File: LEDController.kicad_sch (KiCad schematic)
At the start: 11 parts, among them J9 LED connector, Q3 2N7002K, Q4 2N7002K, Q8 2N7002K

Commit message: Schematic
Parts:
- removed R33, R47, R50: 200Ω, PCM_JLCPCB:R_0603, symbol PCM_JLCPCB-Resistors:0603,200Ω
- added Q10, Q11, Q2, Q3, Q7, Q8: MMBT2222A 1P, PCM_JLCPCB:Q_SOT-23, symbol PCM_JLCPCB-Transistors:NPN,MMBT2222A 1P
- added Q12, Q4, Q9: MMBT5401 200-300, PCM_JLCPCB:Q_SOT-23, symbol PCM_JLCPCB-Transistors:PNP,MMBT5401 200-300
- added R27, R36, R40: 1kΩ, PCM_JLCPCB:R_0402, symbol PCM_JLCPCB-Resistors:0402,1kΩ
- added R28, R32, R35: 100Ω, PCM_JLCPCB:R_0603, symbol PCM_JLCPCB-Resistors:0603,100Ω
- added R29, R37, R41: 10kΩ, PCM_JLCPCB:R_0402, symbol PCM_JLCPCB-Resistors:0402,10kΩ
- added R30, R38, R42: 330Ω, PCM_JLCPCB:R_0402, symbol PCM_JLCPCB-Resistors:0402,330Ω
- added R33, R39, R43: 47Ω, PCM_JLCPCB:R_0402, symbol PCM_JLCPCB-Resistors:0402,47Ω
- renumbered C7 to C6, J9 to J6, Q3 to Q1, Q4 to Q5, Q8 to Q6, R32 to R26, R34 to R31, R49 to R34
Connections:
- net B: now also R40.1; no longer R34.1
- net G: now also R36.1; no longer R31.1
- net GND: now also Q10.2 (E), Q12.2 (E), Q2.2 (E), Q4.2 (E), Q7.2 (E), Q9.2 (E), R29.2, R37.2, R41.2
- net R: now also R27.1; no longer R26.1
- net U_reg: now also Q11.3 (C), Q3.3 (C), Q8.3 (C), R30.1, R38.1, R42.1
- net at Q6.1 (G): now also R35.2
- net at Q5.1 (G): now also R32.2
- net at Q1.1 (G): now also R28.2
- new net: Q7.3 (C), Q8.1 (B), Q9.1 (B), R38.2
- new net: Q8.2 (E), Q9.3 (C), R39.1
- new net: Q2.3 (C), Q3.1 (B), Q4.1 (B), R30.2
- new net: Q7.1 (B), R36.2, R37.1
- new net: Q10.3 (C), Q11.1 (B), Q12.1 (B), R42.2
- new net: Q11.2 (E), Q12.3 (C), R43.1
- new net: Q2.1 (B), R27.2, R29.1
- new net: Q10.1 (B), R40.2, R41.1
- new net: Q3.2 (E), Q4.3 (C), R33.1
- new net S1: R26.1, R28.1, R33.2
- new net S2: R31.1, R32.1, R39.2
- new net S3: R34.1, R35.1, R43.2
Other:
- note added: "IC control"
- note added: "Totem pole driver"
- note removed: "12V"
- moved on the sheet: C6, J6

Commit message: Schematic
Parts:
- removed Q1, Q5, Q6: 2N7002K, PCM_JLCPCB:Q_SOT-23, symbol PCM_JLCPCB-Transistors:NMOS,2N7002K
- added Q1, Q13, Q27: IRF640NPBF, easyeda2kicad:TO-220-3_L10.0-W4.5-P2.54-L, symbol SymboleEasyeda2kicad:IRF640NPBF
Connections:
- net Bin: now also Q27.2 (D)
- net GND: now also Q1.3 (S), Q13.3 (S), Q27.3 (S)
- net Gin: now also Q13.2 (D)
- net Rin: now also Q1.2 (D)
- net at R32.2: now also Q13.1 (G)
- net at R28.2: now also Q1.1 (G)
- net at R35.2: now also Q27.1 (G)
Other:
- moved on the sheet: R26

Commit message: Schematic
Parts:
- removed Q1, Q13, Q27: IRF640NPBF, easyeda2kicad:TO-220-3_L10.0-W4.5-P2.54-L, symbol SymboleEasyeda2kicad:IRF640NPBF
- added Q39, Q42, Q45: CMSA160N10, CMSA160N10:PDFN-8_L5.8-W5.0-P1.27-LS6.1-BL, symbol MojeSymbole:CMSA160N10
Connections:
- net Bin: now also Q45.9 (D)
- net GND: now also R34.1, Q39.1 (S), Q42.1 (S), Q45.1 (S); no longer R34.2
- net Gin: now also Q42.9 (D)
- net Rin: now also Q39.9 (D)
- net S3: now also R34.2; no longer R34.1
- net at R32.2: now also Q42.4 (G)
- net at R35.2: now also Q45.4 (G)
- net at R28.2: now also Q39.4 (G)
- no-connect marks 0 -> 18
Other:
- moved on the sheet: R26, R28, R31, R32, R34, R35

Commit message: reviev by Wojtek
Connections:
- net U_reg: no longer Q11.3 (C), Q3.3 (C), Q8.3 (C), R30.1, R38.1, R42.1
- new net U_IN: Q11.3 (C), Q3.3 (C), Q8.3 (C), R30.1, R38.1, R42.1

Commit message: Schematic touchup
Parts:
- removed Q39, Q42, Q45: CMSA160N10, CMSA160N10:PDFN-8_L5.8-W5.0-P1.27-LS6.1-BL, symbol MojeSymbole:CMSA160N10
- removed R29, R31, R34, R37, R41: 10kΩ, PCM_JLCPCB:R_0402, symbol PCM_JLCPCB-Resistors:0402,10kΩ
- removed R32, R35: 100Ω, PCM_JLCPCB:R_0603, symbol PCM_JLCPCB-Resistors:0603,100Ω
- added Q1, Q13, Q27: AO3400A, PCM_JLCPCB:Q_SOT-23, symbol PCM_JLCPCB-Transistors:NMOS,AO3400A
- added R31, R61: 100Ω, PCM_JLCPCB:R_0603, symbol PCM_JLCPCB-Resistors:0603,100Ω
- added R32, R62: 10kΩ, PCM_JLCPCB:R_0402, symbol PCM_JLCPCB-Resistors:0402,10kΩ
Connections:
- net Bin: now also Q27.3 (D)
- net GND: now also R26.1, Q1.2 (S), Q13.2 (S), Q27.2 (S), R32.1, R62.1; no longer R26.2
- net Gin: now also Q13.3 (D)
- net Rin: now also Q1.3 (D)
- net S1: now also R26.2; no longer R26.1
- net S2: now also R31.1, R32.2
- net S3: now also R61.1, R62.2
- net at R28.2: now also Q1.1 (G)
- new net: Q13.1 (G), R31.2
- new net: Q27.1 (G), R61.2
- no-connect marks 18 -> 0
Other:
- moved on the sheet: R26, R28

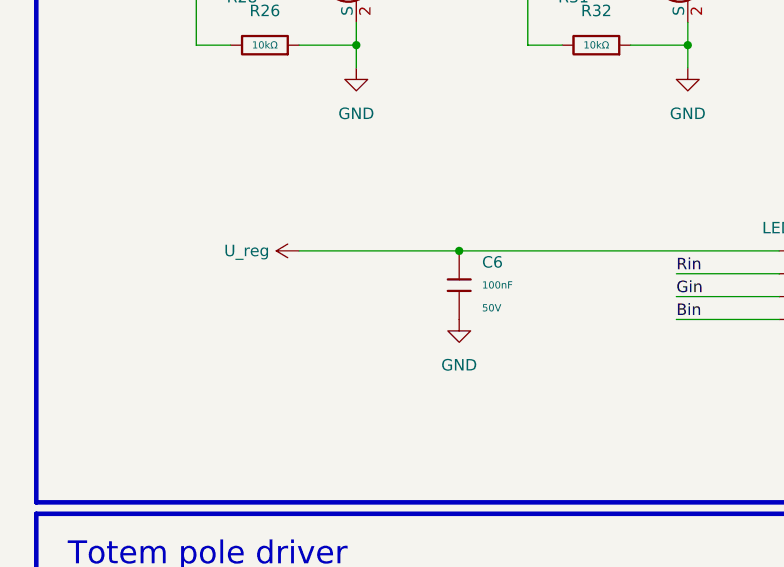
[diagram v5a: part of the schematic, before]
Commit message: PCB design
Hat allows to connect 1 LED tape at a time
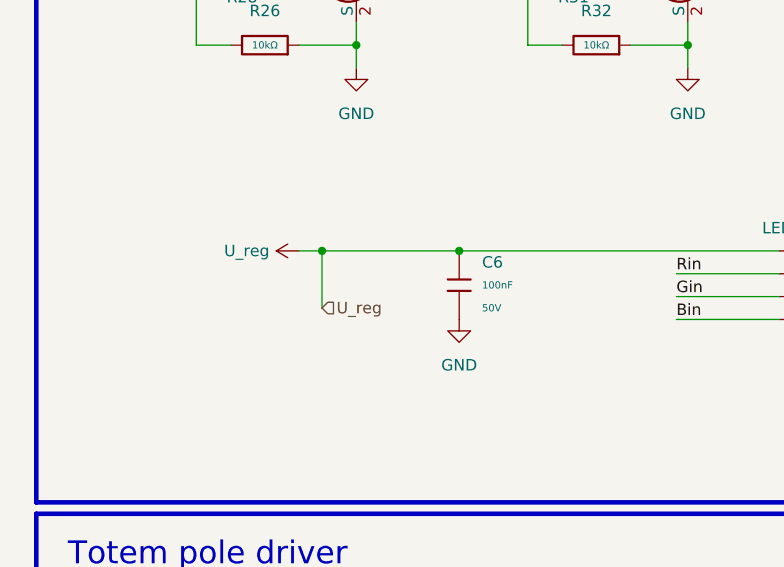
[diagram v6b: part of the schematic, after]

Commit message: PCB addjustments
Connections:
- net U_reg is gone; now on net U_IN: C6.1, J6.1 (Pin_1)
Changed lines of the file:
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@@
 	)
 	(junction
-		(at 46.99 68.58)
-		(diameter 0)
-		(color 0 0 0 0)
-	)
-	(junction
 		(at 106.68 38.1)
 		(diameter 0)
@@
 	(wire
 		(pts
-			(xy 46.99 74.93) (xy 46.99 68.58)
-		)
-		(stroke
-			(width 0)
-			(type default)
-		)
-	)
-	(wire
-		(pts
 			(xy 110.49 45.72) (xy 106.68 45.72)
 		)
@@
 	(wire
 		(pts
-			(xy 46.99 68.58) (xy 62.23 68.58)
+			(xy 44.45 68.58) (xy 62.23 68.58)
 		)
 		(stroke
@@
 	(wire
 		(pts
-			(xy 44.45 68.58) (xy 46.99 68.58)
-		)
-		(stroke
-			(width 0)
-			(type default)
-		)
-	)
-	(wire
-		(pts
 			(xy 62.23 149.86) (xy 77.47 149.86)
 		)
@@
 	(hierarchical_label "U_IN"
 		(shape input)
-		(at 158.75 109.22 90)
+		(at 44.45 68.58 180)
 		(effects
 			(font
 				(size 1.27 1.27)
 			)
-			(justify left)
+			(justify right)
 		)
 	)
-	(hierarchical_label "B"
+	(hierarchical_label "U_IN"
 		(shape input)
-		(at 182.88 135.89 180)
+		(at 158.75 109.22 90)
 		(effects
 			(font
 				(size 1.27 1.27)
 			)
-			(justify right)
+			(justify left)
 		)
 	)
-	(hierarchical_label "U_IN"
+	(hierarchical_label "B"
 		(shape input)
-		(at 77.47 109.22 90)
+		(at 182.88 135.89 180)
 		(effects
 			(font
 				(size 1.27 1.27)
 			)
-			(justify left)
+			(justify right)
 		)
 	)
-	(hierarchical_label "U_reg"
+	(hierarchical_label "U_IN"
 		(shape input)
-		(at 46.99 74.93 0)
+		(at 77.47 109.22 90)
 		(effects
 			(font
@@
 					(unit 1)
 				)
-			)
-		)
-	)
-	(symbol
-		(lib_id "power:+5V")
-		(at 44.45 68.58 90)
-		(mirror x)
-		(unit 1)
-		(body_style 1)
-		(exclude_from_sim no)
-		(in_bom yes)
-		(on_board yes)
-		(in_pos_files yes)
-		(dnp no)
-		(property "Reference" "#PWR073"
-			(at 48.26 68.58 0)
-			(hide yes)
-			(show_name no)
-			(do_not_autoplace no)
-			(effects
-				(font
-					(size 1.27 1.27)
-				)
-			)
-		)
-		(property "Value" "U_reg"
-			(at 41.148 68.58 90)
-			(show_name no)
-			(do_not_autoplace no)
-			(effects
-				(font
-					(size 1.27 1.27)
-				)
-				(justify left)
-			)
-		)
-		(property "Footprint" ""
-			(at 44.45 68.58 0)
-			(hide yes)
-			(show_name no)
-			(do_not_autoplace no)
-			(effects
-				(font
-					(size 1.27 1.27)
-				)
-			)
-		)
-		(property "Datasheet" ""
-			(at 44.45 68.58 0)
-			(hide yes)
-			(show_name no)
-			(do_not_autoplace no)
-			(effects
-				(font
-					(size 1.27 1.27)
-				)
-			)
-		)
-		(property "Description" "Power symbol creates a global label with name \"+5V\""
-			(at 44.45 68.58 0)
-			(hide yes)
-			(show_name no)
-			(do_not_autoplace no)
-			(effects
-				(font
-					(size 1.27 1.27)
-				)
-			)
-		)
-		(pin "1"
-		)
-		(instances
-			(project "MMS3_hat_templates"
-				(path "/6596548a-44e0-46d8-8624-fd71cf4a3e17/f0498328-12ea-48bd-af20-2754c3443d1a"
-					(reference "#PWR073")
-					(unit 1)
-				)
